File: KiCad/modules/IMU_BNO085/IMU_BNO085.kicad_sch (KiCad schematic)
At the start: 7 parts, among them J1 Conn_01x01_Pin, J2 Conn_01x01_Pin, J3 Conn_01x01_Pin, J4 Conn_01x01_Pin, U1 BNO055

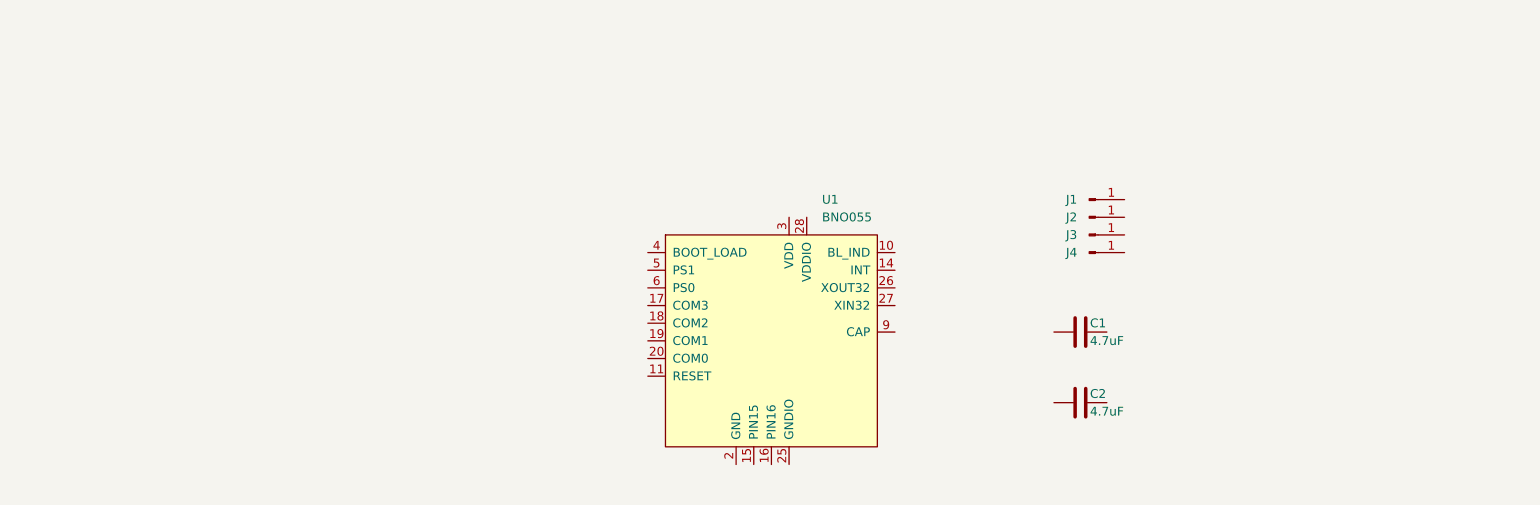
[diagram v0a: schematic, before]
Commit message: finished ads93,commod,drypad,flexpad,jackconn,imubno + plot and render
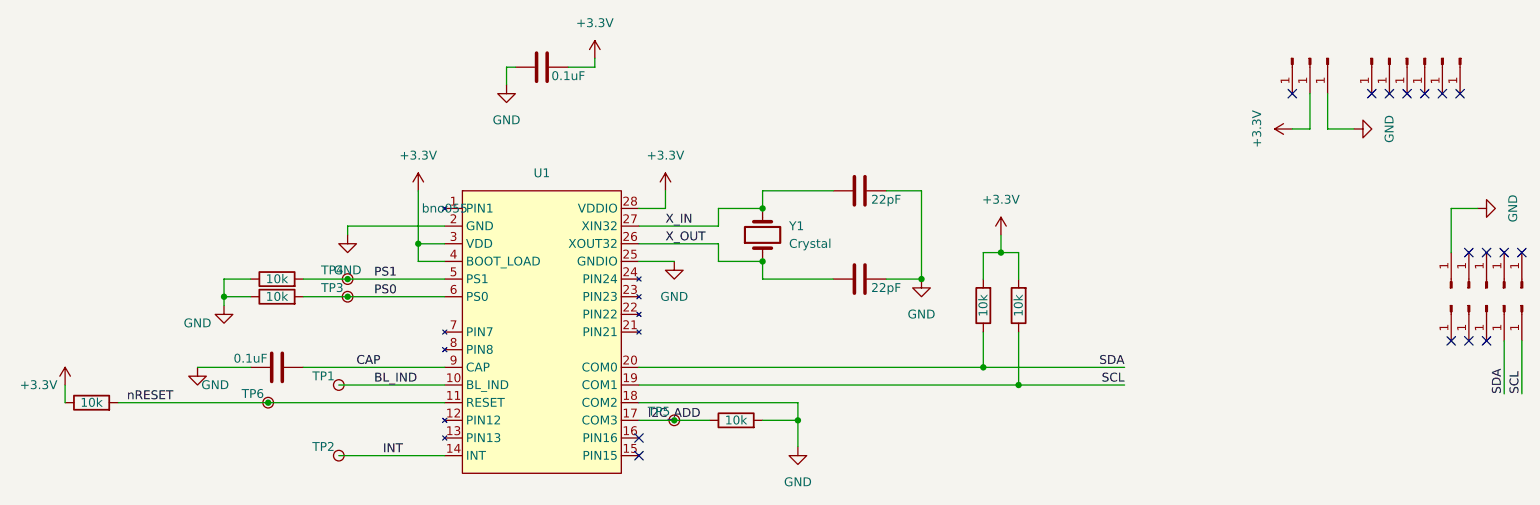
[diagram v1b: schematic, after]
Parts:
- removed U1: BNO055, digikey-footprints:LGA-28_5.2x3.8mm_BNO0055, symbol dk_Motion-Sensors-IMUs-Inertial-Measurement-Units:BNO055
- added C3, C4: 22pF, Capacitor_SMD:C_0402_1005Metric, symbol Device:C
- added J10, J11, J12, J13, J14, J15, J16, J17, J18, J19, J5, J6, J7, J8, J9: Conn_01x01_Pin, Connector_PinHeader_1.27mm:PinHeader_1x01_P1.27mm_Vertical, symbol Connector:Conn_01x01_Pin
- added R1, R2, R3, R4, R5, R6: 10k, Resistor_SMD:R_0402_1005Metric, symbol Device:R
- added TP1, TP2, TP3, TP4, TP5, TP6: TestPoint, 00_Custom:TestPoint_Pad_D1.0mm, symbol 00_custom:TestPoint
- added U1: bno055, digikey-footprints:LGA-28_5.2x3.8mm_BNO0055, symbol 00_custom:BNO055
- added Y1: Crystal, Crystal:Crystal_SMD_3215-2Pin_3.2x1.5mm, symbol Device:Crystal
- C1, C2: value 4.7uF -> 0.1uF
- J1, J2, J3, J4: now left out of the parts list
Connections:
- net SCL: now reaches J3.1 (Pin_1)
- net SCL: now also R5.1, U1.19 (COM1)
- net GND: now reaches C1.1
- net GND: now also C2.2, J4.1 (Pin_1), C3.2, C4.2, J19.1 (Pin_1), R1.2, R2.1, R3.1, U1.18 (COM2), U1.2 (GND), U1.25 (GNDIO)
- net +3.3V: now reaches C1.2
- net +3.3V: now also J1.1 (Pin_1), R4.2, R5.2, R6.1, U1.28 (VDDIO), U1.3 (VDD), U1.4 (BOOT_LOAD)
- net CAP: now reaches C2.1
- net CAP: now also U1.9 (CAP)
- net SDA: now reaches J2.1 (Pin_1)
- net SDA: now also R4.1, U1.20 (COM0)
- new net BL_IND: TP1.1, U1.10 (BL_IND)
- new net I2C_ADD: R1.1, TP5.1, U1.17 (COM3)
- new net INT: TP2.1, U1.14 (INT)
- new net PS0: R2.2, TP3.1, U1.6 (PS0)
- new net PS1: R3.2, TP4.1, U1.5 (PS1)
- new net X_IN: C3.1, U1.27 (XIN32), Y1.2
- new net X_OUT: C4.1, U1.26 (XOUT32), Y1.1
- new net nRESET: R6.2, TP6.1, U1.11 (RESET)
- no-connect marks 0 -> 16
